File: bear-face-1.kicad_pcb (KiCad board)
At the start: 2 copper layers, 301.7 x 112.6 mm, 177 parts, among them J1 Conn_01x04, SW1 SW_Push, U1 Elite-C

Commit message: Elite-C moved
Updated schematic, PCB to reflect Elite-C position change to under spacebar
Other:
- outline, holes or cut-outs redrawn
- board text added: "Bear Face v1 by chemicalwill 01/06/2020"

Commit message: Diodes, silkscreen updated
Changed diodes back to THT diodes to avoid track issues. Intend to use 1N4148 diodes
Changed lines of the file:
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@@
       (net 2 ROW0))
   )
-  (gr_text "Bear Face v1 by chemicalwill\n01/06/2020" (at 219.837 173.228) (layer F.SilkS)
-    (effects (font (size 1.5 1.5) (thickness 0.3)))
+  (gr_text "Bear Face v1 by chemicalwill\n01/06/2020" (at 219.837 173.228) (layer B.SilkS)
+    (effects (font (size 1.5 1.5) (thickness 0.3)) (justify mirror))
   )
   (gr_line (start 59.563 83.439) (end 59.563 72.898) (layer Edge.Cuts) (width 0.12))

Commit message: Mounting holes updated
Used caliper to measure mounting holes on stock PCB, moved mounting holes and surrounding tracks for better fit.
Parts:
- moved D30 15.8 mm to (64.3, 116.0)
- moved D57 6.38 mm to (84.1, 173.0)
- moved H2 3.00 mm to (79.5, 173.1)
- moved H1 2.50 mm to (82.8, 116.1)
- moved H7 1.79 mm to (341.9, 144.0)
- moved H4 0.27 mm to (186.5, 135.3)
- moved H5 0.21 mm to (246.0, 172.8)
- moved H3 0.18 mm to (210.3, 87.6)
- moved H6 0.11 mm to (318.3, 116.1)
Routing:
- net ROW3: track 377.7 -> 394.8 mm
- net Net-(D57-Pad2): track 11.6 -> 18.0 mm
- net Net-(D30-Pad2): track 11.6 -> 6.59 mm
- net GND: track 217.6 -> 220.4 mm

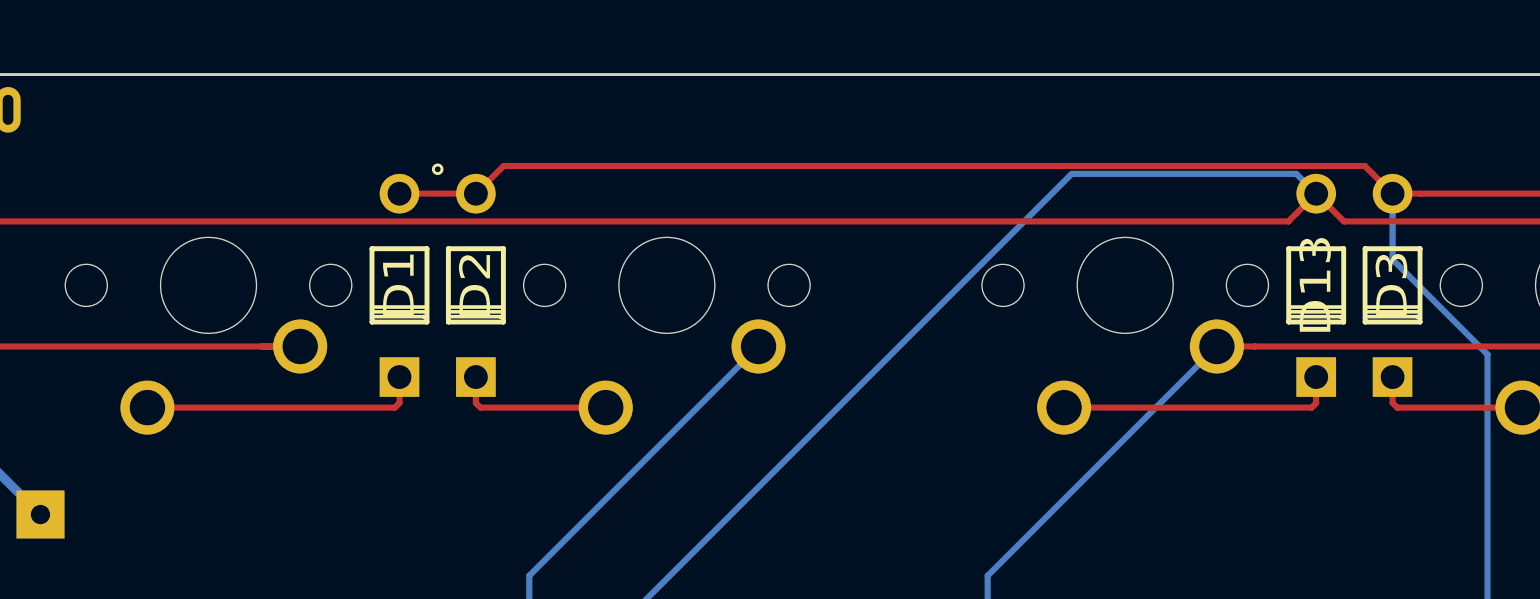
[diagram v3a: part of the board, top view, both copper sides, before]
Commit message: Added hole for plate ground
Stock plate has a hole grounding the plate to the PCB. Added this hole as a 3mm mounting hole (H8)
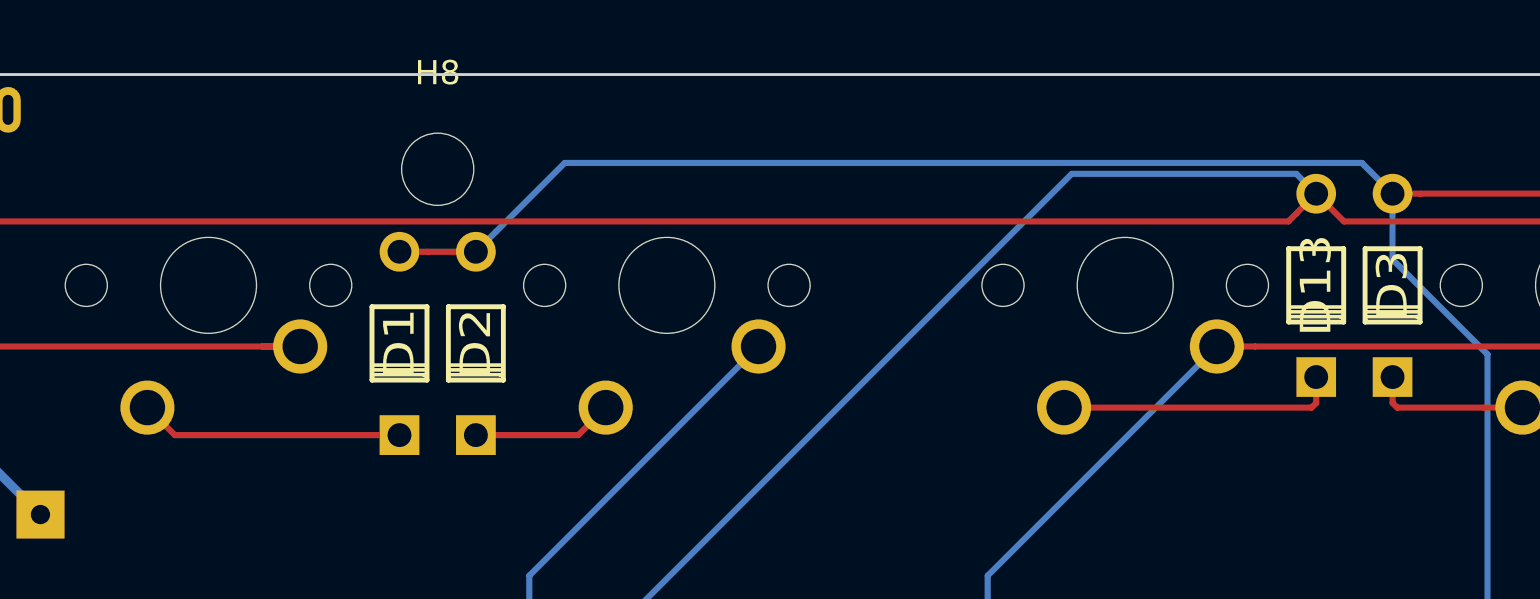
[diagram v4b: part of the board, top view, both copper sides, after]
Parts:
- added H8: Hole, MountingHole:MountingHole_3mm, F.Cu at (105.5, 73.0)
- moved D1 2.41 mm to (103.9, 80.3)
- moved D2 2.41 mm to (107.1, 80.3)
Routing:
- net ROW0: track 386.4 -> 387.5 mm
- net Net-(D1-Pad2): track 11.6 -> 11.0 mm
- net Net-(D2-Pad2): track 6.56 -> 5.87 mm
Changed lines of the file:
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@@
   (general
     (thickness 1.6)
-    (drawings 16)
-    (tracks 867)
+    (drawings 15)
+    (tracks 866)
     (zones 0)
-    (modules 177)
+    (modules 178)
     (nets 116)
   )
@@
     (add_net "Net-(D9-Pad2)")
   )
+  (module MountingHole:MountingHole_3mm (layer F.Cu)
+    (at 105.537 73.025)
+    (descr "Mounting Hole 3mm, no annular")
+    (tags "mounting hole 3mm no annular")
+    (attr virtual)
+    (fp_text reference H8 (at 0 -4) (layer F.SilkS)
+      (effects (font (size 1 1) (thickness 0.15)))
+    )
+    (fp_text value Hole (at 0 4) (layer F.Fab)
+      (effects (font (size 1 1) (thickness 0.15)))
+    )
+    (fp_circle (center 0 0) (end 3.25 0) (layer F.CrtYd) (width 0.05))
+    (fp_circle (center 0 0) (end 3 0) (layer Cmts.User) (width 0.15))
+    (fp_text user %R (at 0.3 0) (layer F.Fab)
+      (effects (font (size 1 1) (thickness 0.15)))
+    )
+    (pad 1 np_thru_hole circle (at 0 0) (size 3 3) (drill 3) (layers *.Cu *.Mask))
+  )
   (module Keebio-Parts:Diode (layer F.Cu)
-    (at 103.9495 77.851 270)
+    (at 103.9495 80.264 270)
     (fp_text reference D1 (at 0 0 90) (layer F.SilkS)
       (effects (font (size 1.27 1.524) (thickness 0.2032)))
@@
   )
   (module Keebio-Parts:Diode (layer F.Cu)
-    (at 107.1245 77.851 270)
+    (at 107.1245 80.264 270)
     (fp_text reference D2 (at 0 0 90) (layer F.SilkS)
       (effects (font (size 1.27 1.524) (thickness 0.2032)))
@@
     (pad 4 thru_hole circle (at -3.25 -2.25 270) (size 1.8 1.8) (drill 1) (layers *.Cu B.Mask))
   )
-  (gr_circle (center 105.537 73.025) (end 105.664 72.898) (layer F.SilkS) (width 0.12))
   (gr_text "Bear Face v1 by chemicalwill\n01/06/2020" (at 219.837 173.228) (layer B.SilkS)
     (effects (font (size 1.5 1.5) (thickness 0.3)) (justify mirror))
@@
   (gr_arc (start 361.061 86.487) (end 361.061 83.439) (angle -180) (layer Edge.Cuts) (width 0.12))
   (gr_arc (start 357.251 72.898) (end 361.061 72.898) (angle -90) (layer Edge.Cuts) (width 0.12))
-  (segment (start 103.9495 82.7405) (end 103.9495 81.661) (width 0.254) (layer F.Cu) (net 1))
-  (segment (start 103.759 82.931) (end 103.9495 82.7405) (width 0.254) (layer F.Cu) (net 1))
-  (segment (start 93.472 82.931) (end 103.759 82.931) (width 0.254) (layer F.Cu) (net 1))
-  (segment (start 103.9495 74.041) (end 107.1245 74.041) (width 0.254) (layer F.Cu) (net 2))
-  (segment (start 144.399001 73.215501) (end 145.2245 74.041) (width 0.254) (layer F.Cu) (net 2))
-  (segment (start 144.071999 72.888499) (end 144.399001 73.215501) (width 0.254) (layer F.Cu) (net 2))
-  (segment (start 108.277001 72.888499) (end 144.071999 72.888499) (width 0.254) (layer F.Cu) (net 2))
-  (segment (start 107.1245 74.041) (end 108.277001 72.888499) (width 0.254) (layer F.Cu) (net 2))
+  (segment (start 94.615 84.074) (end 93.472 82.931) (width 0.254) (layer F.Cu) (net 1))
+  (segment (start 103.9495 84.074) (end 94.615 84.074) (width 0.254) (layer F.Cu) (net 1))
   (segment (start 146.391933 74.041) (end 180.1495 74.041) (width 0.254) (layer F.Cu) (net 2))
   (segment (start 145.2245 74.041) (end 146.391933 74.041) (width 0.254) (layer F.Cu) (net 2))
@@
   (segment (start 146.748019 115.506981) (end 144.78 117.475) (width 0.254) (layer B.Cu) (net 2))
   (segment (start 144.78 132.334) (end 148.336 135.89) (width 0.254) (layer B.Cu) (net 2))
-  (segment (start 107.1245 82.7405) (end 107.1245 81.661) (width 0.254) (layer F.Cu) (net 3))
-  (segment (start 107.315 82.931) (end 107.1245 82.7405) (width 0.254) (layer F.Cu) (net 3))
-  (segment (start 112.522 82.931) (end 107.315 82.931) (width 0.254) (layer F.Cu) (net 3))
+  (segment (start 105.116933 76.454) (end 107.1245 76.454) (width 0.254) (layer F.Cu) (net 2))
+  (segment (start 103.9495 76.454) (end 105.116933 76.454) (width 0.254) (layer F.Cu) (net 2))
+  (segment (start 107.949999 75.628501) (end 107.1245 76.454) (width 0.254) (layer B.Cu) (net 2))
+  (segment (start 143.944991 72.761491) (end 110.817009 72.761491) (width 0.254) (layer B.Cu) (net 2))
+  (segment (start 110.817009 72.761491) (end 107.949999 75.628501) (width 0.254) (layer B.Cu) (net 2))
+  (segment (start 145.2245 74.041) (end 143.944991 72.761491) (width 0.254) (layer B.Cu) (net 2))
+  (segment (start 111.379 84.074) (end 107.1245 84.074) (width 0.254) (layer F.Cu) (net 3))
+  (segment (start 112.522 82.931) (end 111.379 84.074) (width 0.254) (layer F.Cu) (net 3))
   (segment (start 149.03101 82.931) (end 150.622 82.931) (width 0.254) (layer F.Cu) (net 4))
   (segment (start 145.415 82.931) (end 149.03101 82.931) (width 0.254) (layer F.Cu) (net 4))

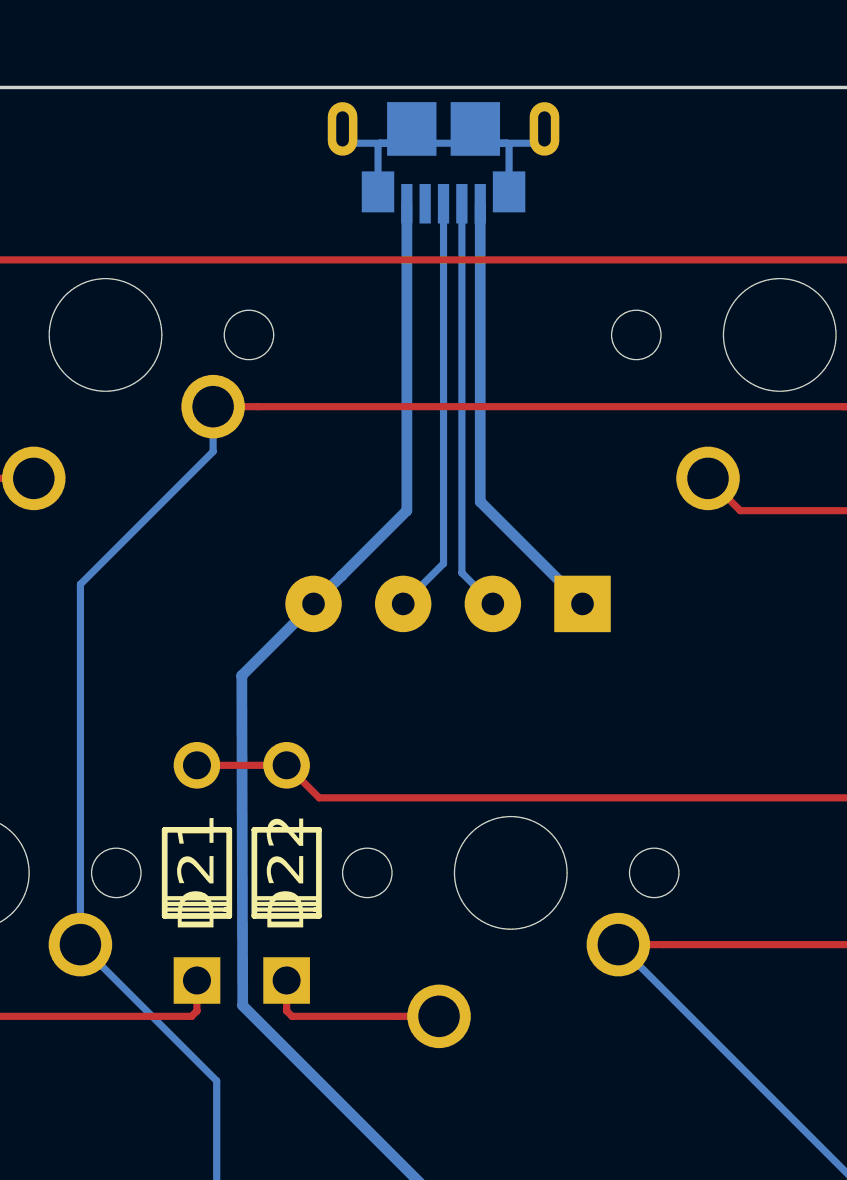
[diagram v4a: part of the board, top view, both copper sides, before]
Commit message: Moved USB connector
Re-measured and moved USB connector to be closer to stock PCB
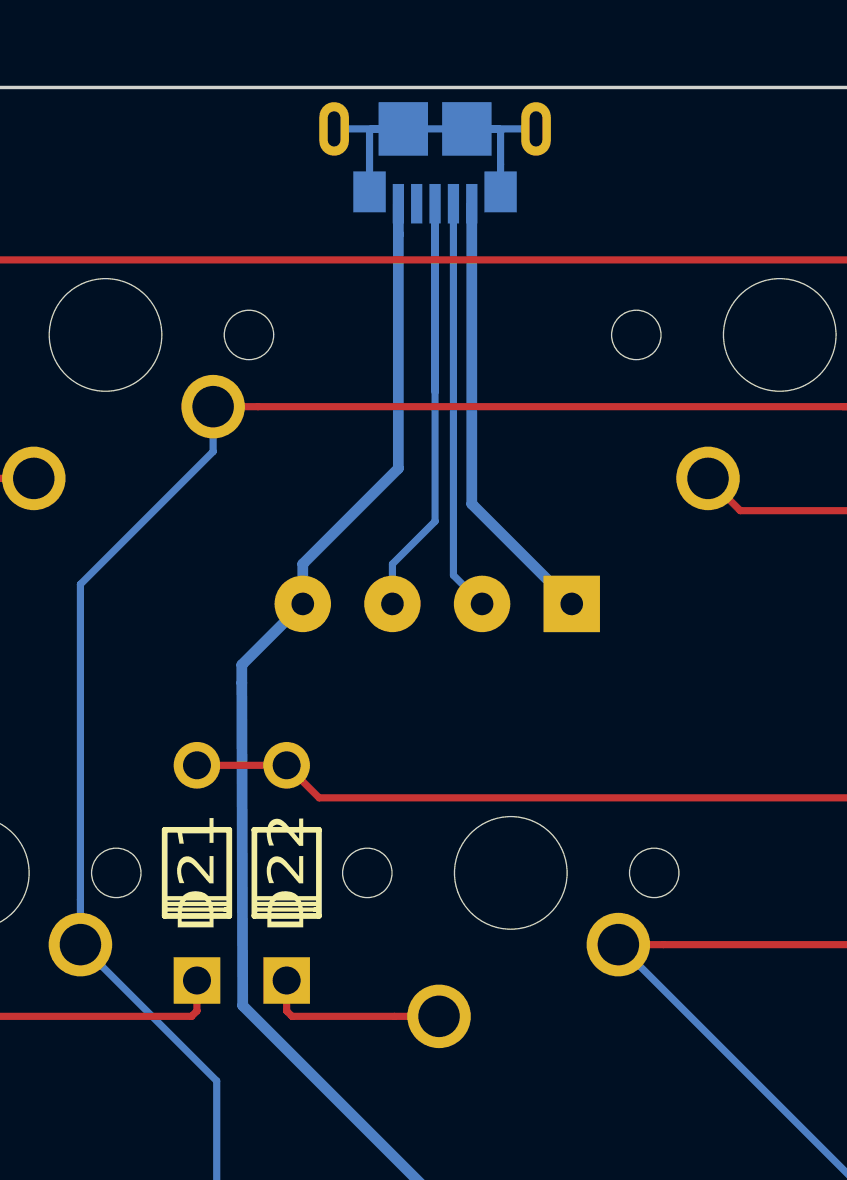
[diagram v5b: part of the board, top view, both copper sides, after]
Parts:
- moved J1 0.38 mm to (88.6, 87.4)
- moved USB1 0.30 mm to (83.8, 71.8)
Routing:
- net /D+: track 14.8 -> 21.5 mm
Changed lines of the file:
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@@
     (thickness 1.6)
     (drawings 15)
-    (tracks 866)
+    (tracks 870)
     (zones 0)
     (modules 178)
@@
   )
   (module Connector_USB:USB_Micro-B_GCT_USB3076-30-A (layer B.Cu)
-    (at 84.10575 71.755)
+    (at 83.80575 71.755)
     (descr "GCT Micro USB https://gct.co/files/drawings/usb3076.pdf")
     (tags "Micro-USB SMD Typ-B GCT")
@@
   )
   (module Connector_Wire:SolderWirePad_1x04_P3.175mm_Drill0.8mm (layer B.Cu)
-    (at 89.027 87.376 180)
+    (at 88.646 87.376 180)
     (descr "Wire solder connection")
     (tags connector)
@@
   (segment (start 269.24 178.181) (end 269.0495 177.9905) (width 0.254) (layer F.Cu) (net 92))
   (segment (start 274.447 178.181) (end 269.24 178.181) (width 0.254) (layer F.Cu) (net 92))
-  (segment (start 80.501489 86.376511) (end 79.502 87.376) (width 0.381) (layer B.Cu) (net 93))
-  (segment (start 82.80575 84.07225) (end 80.501489 86.376511) (width 0.381) (layer B.Cu) (net 93))
-  (segment (start 82.80575 73.205) (end 82.80575 84.07225) (width 0.381) (layer B.Cu) (net 93))
   (segment (start 163.322 179.324) (end 165.862 179.324) (width 0.381) (layer F.Cu) (net 93))
   (segment (start 168.402 164.084) (end 164.595199 167.890801) (width 0.381) (layer F.Cu) (net 93))
@@
   (segment (start 168.402 176.784) (end 165.862 179.324) (width 0.381) (layer B.Cu) (net 93))
   (segment (start 168.402 164.084) (end 168.402 176.784) (width 0.381) (layer B.Cu) (net 93))
-  (segment (start 76.962 89.916) (end 79.502 87.376) (width 0.381) (layer B.Cu) (net 93))
-  (segment (start 76.99375 101.6) (end 76.962 89.916) (width 0.381) (layer B.Cu) (net 93))
   (segment (start 86.51875 111.125) (end 76.99375 101.6) (width 0.381) (layer B.Cu) (net 93))
   (segment (start 86.51875 123.11925) (end 86.51875 111.125) (width 0.381) (layer B.Cu) (net 93))
   (segment (start 83.44325 126.19475) (end 86.51875 123.11925) (width 0.381) (layer B.Cu) (net 93))
-  (segment (start 84.10575 85.94725) (end 82.677 87.376) (width 0.254) (layer B.Cu) (net 94))
-  (segment (start 84.10575 73.205) (end 84.10575 85.94725) (width 0.254) (layer B.Cu) (net 94))
-  (segment (start 84.75575 86.27975) (end 85.852 87.376) (width 0.254) (layer B.Cu) (net 95))
-  (segment (start 84.75575 73.205) (end 84.75575 86.27975) (width 0.254) (layer B.Cu) (net 95))
-  (segment (start 85.40575 83.75475) (end 89.027 87.376) (width 0.381) (layer B.Cu) (net 96))
-  (segment (start 85.40575 73.205) (end 85.40575 83.75475) (width 0.381) (layer B.Cu) (net 96))
+  (segment (start 79.121 87.376) (end 76.962 89.535) (width 0.381) (layer B.Cu) (net 93))
+  (segment (start 76.99375 101.6) (end 76.962 90.17) (width 0.381) (layer B.Cu) (net 93))
+  (segment (start 76.962 90.17) (end 76.962 89.535) (width 0.381) (layer B.Cu) (net 93))
+  (segment (start 82.50575 82.577758) (end 82.50575 74.286) (width 0.381) (layer B.Cu) (net 93))
+  (segment (start 82.50575 74.286) (end 82.50575 73.205) (width 0.381) (layer B.Cu) (net 93))
+  (segment (start 79.121 85.962508) (end 82.50575 82.577758) (width 0.381) (layer B.Cu) (net 93))
+  (segment (start 79.121 87.376) (end 79.121 85.962508) (width 0.381) (layer B.Cu) (net 93))
+  (segment (start 83.80575 73.205) (end 83.80575 79.86875) (width 0.254) (layer B.Cu) (net 94))
+  (segment (start 83.80575 74.159) (end 83.80575 73.205) (width 0.254) (layer B.Cu) (net 94))
+  (segment (start 83.80575 84.452758) (end 83.80575 74.159) (width 0.254) (layer B.Cu) (net 94))
+  (segment (start 82.296 85.962508) (end 83.80575 84.452758) (width 0.254) (layer B.Cu) (net 94))
+  (segment (start 82.296 87.376) (end 82.296 85.962508) (width 0.254) (layer B.Cu) (net 94))
+  (segment (start 84.45575 86.36075) (end 85.471 87.376) (width 0.254) (layer B.Cu) (net 95))
+  (segment (start 84.45575 73.205) (end 84.45575 86.36075) (width 0.254) (layer B.Cu) (net 95))
+  (segment (start 85.10575 83.83575) (end 88.646 87.376) (width 0.381) (layer B.Cu) (net 96))
+  (segment (start 85.10575 73.205) (end 85.10575 83.83575) (width 0.381) (layer B.Cu) (net 96))
   (segment (start 272.86299 80.391) (end 290.322 80.391) (width 0.254) (layer F.Cu) (net 97))
   (segment (start 271.272 80.391) (end 272.86299 80.391) (width 0.254) (layer F.Cu) (net 97))
@@
   (segment (start 72.23125 156.707962) (end 82.896579 167.373291) (width 0.254) (layer F.Cu) (net 107))
   (segment (start 72.23125 148.40675) (end 72.23125 156.707962) (width 0.254) (layer F.Cu) (net 107))
-  (segment (start 80.53075 71.063) (end 82.98075 71.063) (width 0.254) (layer B.Cu) (net 109))
-  (segment (start 82.98075 71.063) (end 85.23075 71.063) (width 0.254) (layer B.Cu) (net 109))
-  (segment (start 85.23075 71.063) (end 87.68075 71.063) (width 0.254) (layer B.Cu) (net 109))
-  (segment (start 86.42575 72.314) (end 86.42575 73.293) (width 0.254) (layer B.Cu) (net 109))
-  (segment (start 86.42575 71.129) (end 86.42575 72.314) (width 0.254) (layer B.Cu) (net 109))
-  (segment (start 86.35975 71.063) (end 86.42575 71.129) (width 0.254) (layer B.Cu) (net 109))
-  (segment (start 85.23075 71.063) (end 86.35975 71.063) (width 0.254) (layer B.Cu) (net 109))
-  (segment (start 81.78575 72.314) (end 81.78575 73.293) (width 0.254) (layer B.Cu) (net 109))
-  (segment (start 81.85175 71.063) (end 81.78575 71.129) (width 0.254) (layer B.Cu) (net 109))
-  (segment (start 81.78575 71.129) (end 81.78575 72.314) (width 0.254) (layer B.Cu) (net 109))
-  (segment (start 82.98075 71.063) (end 81.85175 71.063) (width 0.254) (layer B.Cu) (net 109))
+  (segment (start 80.23075 70.555) (end 82.68075 70.555) (width 0.254) (layer B.Cu) (net 109))
+  (segment (start 81.55175 70.555) (end 82.68075 70.555) (width 0.254) (layer B.Cu) (net 109))
+  (segment (start 81.48575 70.621) (end 81.55175 70.555) (width 0.254) (layer B.Cu) (net 109))
+  (segment (start 81.48575 72.785) (end 81.48575 70.621) (width 0.254) (layer B.Cu) (net 109))
+  (segment (start 82.68075 70.555) (end 84.93075 70.555) (width 0.254) (layer B.Cu) (net 109))
+  (segment (start 84.93075 70.555) (end 87.38075 70.555) (width 0.254) (layer B.Cu) (net 109))
+  (segment (start 86.05975 70.555) (end 86.12575 70.621) (width 0.254) (layer B.Cu) (net 109))
+  (segment (start 86.12575 71.806) (end 86.12575 72.785) (width 0.254) (layer B.Cu) (net 109))
+  (segment (start 86.12575 70.621) (end 86.12575 71.806) (width 0.254) (layer B.Cu) (net 109))
+  (segment (start 84.93075 70.555) (end 86.05975 70.555) (width 0.254) (layer B.Cu) (net 109))
 )
